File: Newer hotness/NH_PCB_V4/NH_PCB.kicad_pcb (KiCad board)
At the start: 2 copper layers, 101.6 x 63.5 mm, 31 parts, among them J1 Xbee-Conn, J2 STRAT_CONN, J3 Pow_byp, J4 BARREL_JACK, J5 SPI_debug, J6 I2C_Debug, U1 Teensy3.6, U2 ACCL_BOB_A1413, U3 10DOF_A1604

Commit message: telemetry PCB updates
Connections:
- net /Xbee_1 renamed /GPS-FIX
- J1 pad 10: /Xbee_4 -> /Xbee_ATTN
- J1 pad 8: /Xbee_2 -> /CLK
- J1 pad 9: /Xbee_3 -> /Xbee_SS
- U1 pad 17: /Xbee_2 -> /Xbee_ATTN
- U1 pad 18: /Xbee_3 -> Net-(U1-Pad18)
- U1 pad 19: /Xbee_4 -> Net-(U1-Pad19)
- U1 pad 42: Net-(U1-Pad42) -> /Xbee_SS
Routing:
- net /Xbee_SS: track 0.00 -> 54.1 mm
- net /CLK: track 97.8 -> 139.5 mm
- net /Xbee_3: track 28.9 -> 0.00 mm
- net /Xbee_ATTN: track 0.00 -> 28.6 mm
- net /Xbee_2: track 26.0 -> 0.00 mm
- net /Xbee_4: track 25.6 -> 0.00 mm
- net /Vin: track 77.0 -> 81.9 mm
- net /SDA: track 57.6 -> 61.6 mm
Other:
- board text added: "330"
- board text removed: "15-6V"
- board text removed: "180"

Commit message: updated PCB files
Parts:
- added BZ1: Buzzer, adafruit_BOBs:Buzzer_A1536, F.Cu at (184.8, 96.9)
- moved Reg1 10.9 mm to (184.2, 107.9)
- moved C3 3.32 mm to (195.0, 107.8)
- moved J4 0.50 mm to (199.5, 98.1)
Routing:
- net GND: track 181.7 -> 150.1 mm
- net Net-(BZ1-Pad1): track 0.00 -> 31.1 mm
- net /DOUT: track 81.1 -> 84.2 mm
- net /3.3V: track 172.3 -> 174.2 mm
- net Net-(C3-Pad1): track 25.7 -> 27.4 mm
- net Net-(D3-Pad1): track 25.8 -> 24.7 mm
- net /CLK: track 139.5 -> 140.6 mm
- net /DIN: track 108.8 -> 109.5 mm
- net /Vin: track 81.9 -> 82.3 mm, vias 1 -> 2
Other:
- rule via_min_drill: 0.3 -> 0.381

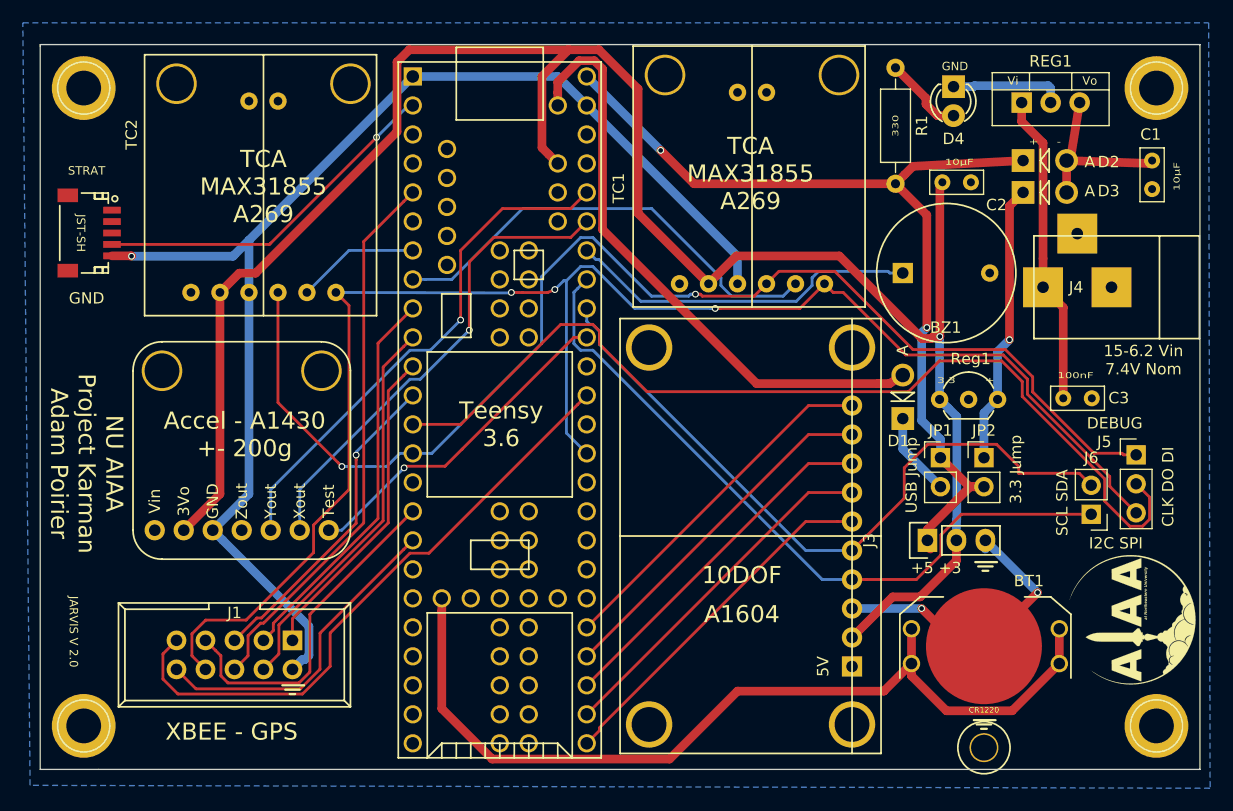
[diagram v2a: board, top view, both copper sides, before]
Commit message: finalized PCB layouts for the hotnesses... also  for the love of god rename these rockets
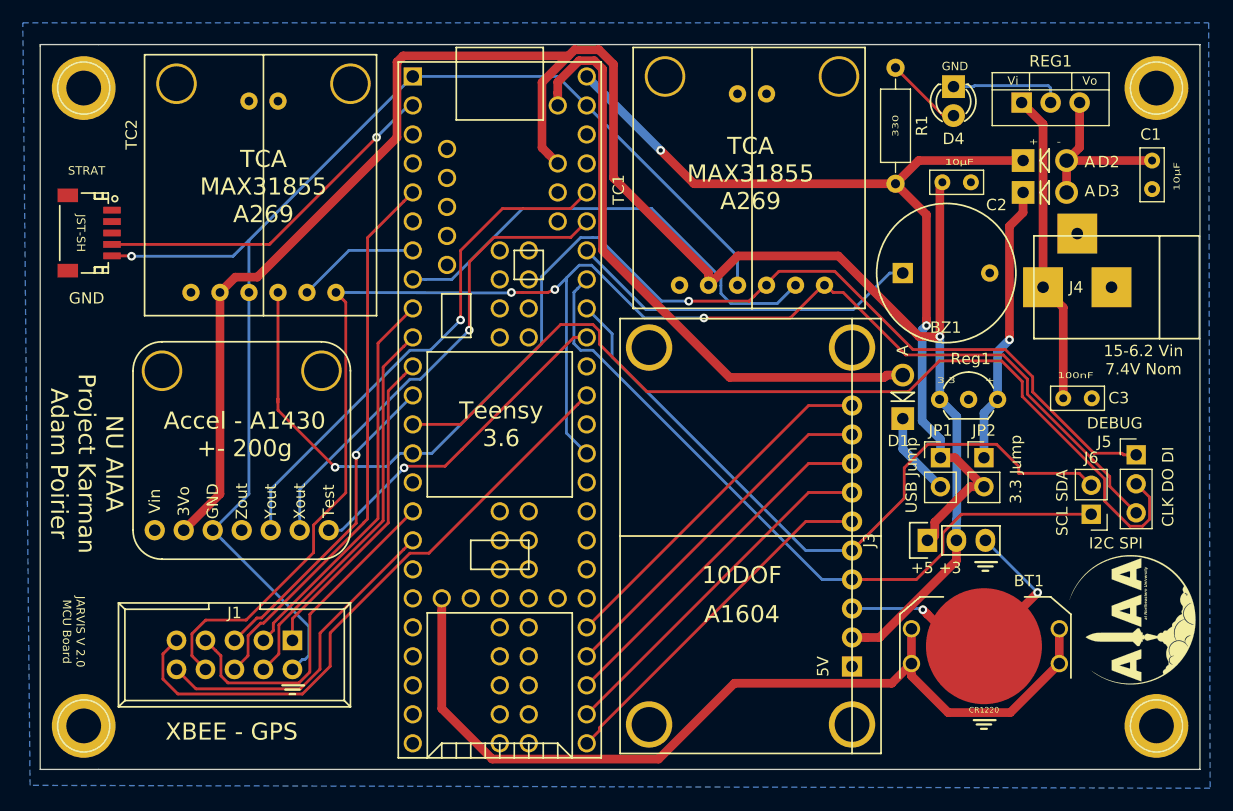
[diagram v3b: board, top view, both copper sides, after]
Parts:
- removed the REF** at (188.1, 138.4)
- moved TC1 0.13 mm to (177.7, 77.1)
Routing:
- net Net-(C1-Pad1): track 15.7 -> 16.7 mm
- net /DIN: track 109.5 -> 110.5 mm
- net /CS-TC1: track 40.1 -> 41.0 mm
- net /CLK: track 140.6 -> 141.4 mm
- net /VUSB: track 53.2 -> 53.9 mm
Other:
- net class Default: via_dia 0.6 -> 0.762; via_drill 0.4 -> 0.381
- board text added: "JARVIS V 2.0 MCU Board"
- board text removed: "JARVIS V 2.0"

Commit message: Finalized NH PCBs
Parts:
- added J7: Pow_in, Pin_Headers:Pin_Header_Straight_1x02, F.Cu at (204.3, 87.6)
- moved C1 3.02 mm to (199.8, 87.3)
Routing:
- net Net-(C3-Pad1): track 27.4 -> 46.5 mm
- net Net-(C1-Pad1): track 16.7 -> 13.5 mm
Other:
- board text added: "+"
- board text added: "- +"
- board text added: "Pow in"
- board text removed: "+ -"
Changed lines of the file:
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@@
 (kicad_pcb (version 4) (host pcbnew 4.0.6)
   (general
-    (links 75)
+    (links 77)
     (no_connects 0)
-    (area 105.359999 76.784999 207.060001 140.385001)
+    (area 103.886 74.93 207.899001 141.986001)
     (thickness 1.6)
-    (drawings 51)
-    (tracks 383)
+    (drawings 53)
+    (tracks 390)
     (zones 0)
-    (modules 31)
+    (modules 32)
     (nets 100)
   )
@@
   )
   (setup
-    (last_trace_width 0.762)
+    (last_trace_width 0.25)
     (user_trace_width 0.762)
     (trace_clearance 0.2)
@@
     (pad_to_mask_clearance 0)
     (aux_axis_origin 0 0)
-    (visible_elements FFFFEF7F)
+    (visible_elements FFFEEF7F)
     (pcbplotparams
       (layerselection 0x010f0_80000001)
@@
     (descr "Diode, DO-41, SOD81, Vertical, Anode Up,")
     (tags "Diode, DO-41, SOD81, Vertical, Anode Up, 1N4007, SB140,")
-    (fp_text reference D2 (at 7.493 0.127) (layer F.SilkS)
+    (fp_text reference D2 (at 5.9182 -1.7272) (layer F.SilkS)
       (effects (font (size 1 1) (thickness 0.15)))
     )
@@
     (descr "Diode, DO-41, SOD81, Vertical, Anode Up,")
     (tags "Diode, DO-41, SOD81, Vertical, Anode Up, 1N4007, SB140,")
-    (fp_text reference D3 (at 7.493 -0.127) (layer F.SilkS)
+    (fp_text reference D3 (at 0.127 2.032) (layer F.SilkS)
       (effects (font (size 1 1) (thickness 0.15)))
     )
@@
   )
   (module Capacitors_THT:C_Rect_L4.6mm_W2.0mm_P2.50mm_MKS02_FKP02 (layer F.Cu)
-    (at 202.819 86.995 270)
+    (at 199.8218 87.3398 270)
     (descr "C, Rect series, Radial, pin pitch=2.50mm, , length*width=4.6*2mm^2, Capacitor, http://www.wima.de/DE/WIMA_MKS_02.pdf")
     (tags "C Rect series Radial pin pitch 2.50mm  length 4.6mm width 2mm Capacitor")
@@
       (net 77 GND))
   )
+  (module Pin_Headers:Pin_Header_Straight_1x02 (layer F.Cu)
+    (at 204.3176 87.5792)
+    (descr "Through hole pin header")
+    (tags "pin header")
+    (fp_text reference J7 (at 0 -5.1) (layer F.SilkS)
+      (effects (font (size 1 1) (thickness 0.15)))
+    )
+    (fp_text value Pow_in (at 0 -3.1) (layer F.Fab)
+      (effects (font (size 1 1) (thickness 0.15)))
+    )
+    (fp_line (start 1.27 1.27) (end 1.27 3.81) (layer F.SilkS) (width 0.15))
+    (fp_line (start 1.55 -1.55) (end 1.55 0) (layer F.SilkS) (width 0.15))
+    (fp_line (start -1.75 -1.75) (end -1.75 4.3) (layer F.CrtYd) (width 0.05))
+    (fp_line (start 1.75 -1.75) (end 1.75 4.3) (layer F.CrtYd) (width 0.05))
+    (fp_line (start -1.75 -1.75) (end 1.75 -1.75) (layer F.CrtYd) (width 0.05))
+    (fp_line (start -1.75 4.3) (end 1.75 4.3) (layer F.CrtYd) (width 0.05))
+    (fp_line (start 1.27 1.27) (end -1.27 1.27) (layer F.SilkS) (width 0.15))
+    (fp_line (start -1.55 0) (end -1.55 -1.55) (layer F.SilkS) (width 0.15))
+    (fp_line (start -1.55 -1.55) (end 1.55 -1.55) (layer F.SilkS) (width 0.15))
+    (fp_line (start -1.27 1.27) (end -1.27 3.81) (layer F.SilkS) (width 0.15))
+    (fp_line (start -1.27 3.81) (end 1.27 3.81) (layer F.SilkS) (width 0.15))
+    (pad 1 thru_hole rect (at 0 0) (size 2.032 2.032) (drill 1.016) (layers *.Cu *.Mask)
+      (net 80 "Net-(C3-Pad1)"))
+    (pad 2 thru_hole oval (at 0 2.54) (size 2.032 2.032) (drill 1.016) (layers *.Cu *.Mask)
+      (net 77 GND))
+    (model Pin_Headers.3dshapes/Pin_Header_Straight_1x02.wrl
+      (at (xyz 0 -0.05 0))
+      (scale (xyz 1 1 1))
+      (rotate (xyz 0 0 90))
+    )
+  )
+  (gr_text + (at 204.343 85.344) (layer F.SilkS)
+    (effects (font (size 0.522 0.738) (thickness 0.1222)))
+  )
+  (gr_text "Pow in" (at 204.2922 84.3788) (layer F.SilkS)
+    (effects (font (size 0.522 0.738) (thickness 0.1222)))
+  )
   (gr_text JST-SH (at 108.966 93.345 270) (layer F.SilkS)
     (effects (font (size 0.738 0.738) (thickness 0.1222)))
@@
     (effects (font (size 1.5 1.5) (thickness 0.3)))
   )
-  (gr_text 10µF (at 204.978 88.392 90) (layer F.SilkS)
+  (gr_text 10µF (at 201.6506 88.2142 90) (layer F.SilkS)
     (effects (font (size 0.522 0.738) (thickness 0.1222)))
   )
@@
     (effects (font (size 0.522 0.738) (thickness 0.1222)))
   )
-  (gr_text "+     -" (at 193.421 85.344) (layer F.SilkS)
+  (gr_text "-     +" (at 193.421 85.344) (layer F.SilkS)
     (effects (font (size 0.522 0.738) (thickness 0.1222)))
   )
@@
   (segment (start 187.266001 80.433999) (end 187.182 80.518) (width 0.25) (layer B.Cu) (net 77))
   (segment (start 187.182 80.518) (end 185.42 80.518) (width 0.25) (layer B.Cu) (net 77))
+  (segment (start 199.8218 87.3398) (end 195.6708 87.3398) (width 0.762) (layer F.Cu) (net 78))
+  (segment (start 195.6708 87.3398) (end 195.326 86.995) (width 0.762) (layer F.Cu) (net 78))
   (segment (start 195.326 89.789) (end 195.326 86.995) (width 0.762) (layer F.Cu) (net 78))
-  (segment (start 195.326 86.995) (end 202.819 86.995) (width 0.762) (layer F.Cu) (net 78))
   (segment (start 196.469 81.915) (end 196.469 85.852) (width 0.762) (layer F.Cu) (net 78))
   (segment (start 196.469 85.852) (end 195.326 86.995) (width 0.762) (layer F.Cu) (net 78))
-  (segment (start 202.565 87.249) (end 202.819 86.995) (width 0.25) (layer F.Cu) (net 78) (status 30))
   (segment (start 195.707 86.614) (end 195.326 86.995) (width 0.25) (layer F.Cu) (net 78) (status 30))
   (segment (start 117.983 119.38) (end 121.158 116.205) (width 0.762) (layer F.Cu) (net 79))
@@
   (segment (start 185.674 120.269) (end 185.674 120.1166) (width 0.25) (layer F.Cu) (net 79) (status 30))
   (segment (start 185.674 120.4214) (end 185.674 120.269) (width 0.25) (layer F.Cu) (net 79) (status 30))
+  (segment (start 197.358 80.137) (end 191.505 80.137) (width 0.762) (layer F.Cu) (net 80))
+  (segment (start 191.505 80.137) (end 191.389 80.253) (width 0.762) (layer F.Cu) (net 80))
+  (segment (start 191.389 80.253) (end 191.389 81.915) (width 0.762) (layer F.Cu) (net 80))
+  (segment (start 199.3138 82.0928) (end 197.358 80.137) (width 0.762) (layer F.Cu) (net 80))
+  (segment (start 199.3138 84.3534) (end 199.3138 82.0928) (width 0.762) (layer F.Cu) (net 80))
+  (segment (start 204.3176 87.5792) (end 202.5396 87.5792) (width 0.762) (layer F.Cu) (net 80))
+  (segment (start 202.5396 87.5792) (end 199.3138 84.3534) (width 0.762) (layer F.Cu) (net 80))
   (segment (start 195.0358 107.823) (end 195.0358 99.86708) (width 0.762) (layer F.Cu) (net 80))
   (segment (start 195.0358 99.86708) (end 193.26352 98.0948) (width 0.762) (layer F.Cu) (net 80))
